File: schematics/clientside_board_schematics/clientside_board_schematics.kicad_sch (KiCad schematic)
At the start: 21 parts, among them J1 Comm Status LED, J2 12V Power Input, J3 UART Connector, J4 12V Output, J5 5V Output, J6 Potentiometer Connector, J7 Fire Button Connector, J8 Keylock Switch Connector, J9 LCD Connector, T1 VXO7805-1000

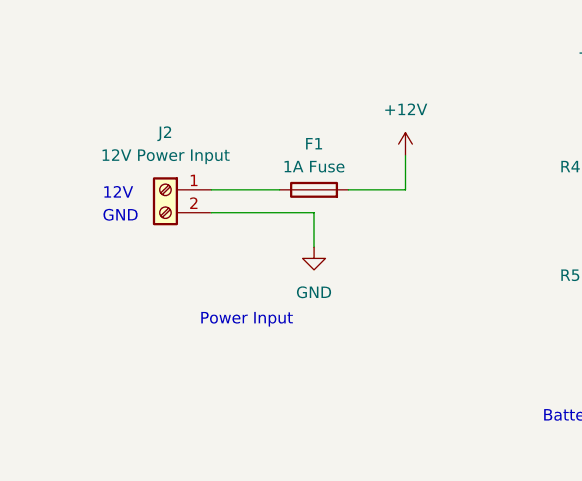
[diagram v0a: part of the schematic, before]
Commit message: Add clientside board routing
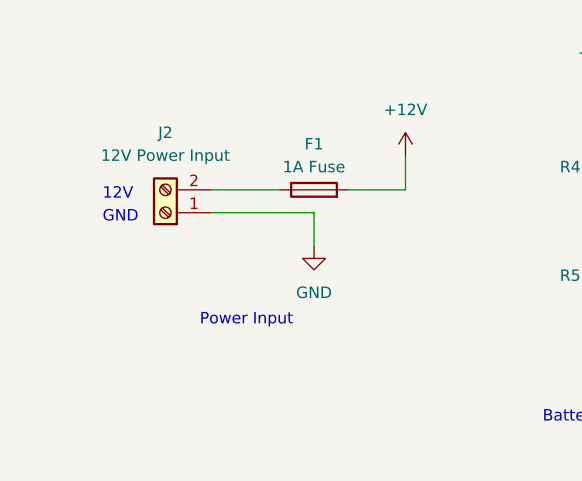
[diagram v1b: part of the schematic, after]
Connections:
- net GND: now also J2.1 (Pin_1); no longer J2.2 (Pin_2)
- net at F1.1: now also J2.2 (Pin_2); no longer J2.1 (Pin_1)
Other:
- moved on the sheet: J2
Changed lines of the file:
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@@
+    (stroke (width 0) (type default))
+  )
+  (wire (pts (xy 50.8 130.81) (xy 53.34 130.81))
+    (stroke (width 0) (type default))
+  )
+  (wire (pts (xy 86.36 44.45) (xy 86.36 45.72))
+    (stroke (width 0) (type default))
+  )
+  (wire (pts (xy 158.75 35.56) (xy 168.91 35.56))
+    (stroke (width 0) (type default))
+  )
+  (wire (pts (xy 139.7 166.37) (xy 139.7 168.91))
+    (stroke (width 0) (type default))
+  )
+  (wire (pts (xy 160.02 91.44) (xy 175.26 91.44))
+    (stroke (width 0) (type default))
+  )
+  (wire (pts (xy 234.95 97.79) (xy 237.49 97.79))
+    (stroke (width 0) (type default))
+  )
+  (wire (pts (xy 233.68 115.57) (xy 237.49 115.57))
+    (stroke (width 0) (type default))
+  )
+  (wire (pts (xy 233.68 110.49) (xy 237.49 110.49))
+    (stroke (width 0) (type default))
+  )
+  (wire (pts (xy 62.23 93.98) (xy 62.23 95.25))
+    (stroke (width 0) (type default))
+  )
+  (wire (pts (xy 113.03 102.87) (xy 113.03 105.41))
+    (stroke (width 0) (type default))
+  )
+  (wire (pts (xy 92.71 116.84) (xy 92.71 123.19))
+    (stroke (width 0) (type default))
+  )
+  (wire (pts (xy 121.92 165.1) (xy 121.92 167.64))
+    (stroke (width 0) (type default))
+  )
+  (wire (pts (xy 123.19 35.56) (xy 133.35 35.56))
+    (stroke (width 0) (type default))
+  )
+  (wire (pts (xy 45.72 91.44) (xy 62.23 91.44))
+    (stroke (width 0) (type default))
+  )
+  (wire (pts (xy 133.35 33.02) (xy 133.35 35.56))
+    (stroke (width 0) (type default))
+  )
+  (wire (pts (xy 234.95 125.73) (xy 234.95 123.19))
+    (stroke (width 0) (type default))
+  )
+  (wire (pts (xy 92.71 96.52) (xy 92.71 105.41))
+    (stroke (width 0) (type default))
+  )
+  (wire (pts (xy 36.83 120.65) (xy 41.91 120.65))
+    (stroke (width 0) (type default))
+  )
+  (wire (pts (xy 214.63 34.29) (xy 229.87 34.29))
+    (stroke (width 0) (type default))
+  )
+  (wire (pts (xy 133.35 38.1) (xy 133.35 41.91))
+    (stroke (width 0) (type default))
+  )
+  (wire (pts (xy 50.8 114.3) (xy 53.34 114.3))
+    (stroke (width 0) (type default))
+  )
+  (wire (pts (xy 50.8 123.19) (xy 53.34 123.19))
+    (stroke (width 0) (type default))
+  )
+  (wire (pts (xy 175.26 86.36) (xy 175.26 83.82))
+    (stroke (width 0) (type default))
+  )
+  (wire (pts (xy 234.95 123.19) (xy 237.49 123.19))
+    (stroke (width 0) (type default))
+  )
+  (wire (pts (xy 168.91 30.48) (xy 168.91 35.56))
+    (stroke (width 0) (type default))
+  )
+  (wire (pts (xy 41.91 125.73) (xy 41.91 130.81))
+    (stroke (width 0) (type default))
+  )
+  (wire (pts (xy 229.87 34.29) (xy 229.87 36.83))
+    (stroke (width 0) (type default))
+  )
+  (wire (pts (xy 121.92 96.52) (xy 121.92 105.41))
     (stroke (width 0) (type default))
   )
   (wire (pts (xy 43.18 43.18) (xy 50.8 43.18))
-    (stroke (width 0) (type default))
-  )
-  (wire (pts (xy 50.8 130.81) (xy 53.34 130.81))
-    (stroke (width 0) (type default))
-  )
-  (wire (pts (xy 86.36 44.45) (xy 86.36 45.72))
-    (stroke (width 0) (type default))
-  )
-  (wire (pts (xy 158.75 35.56) (xy 168.91 35.56))
-    (stroke (width 0) (type default))
-  )
-  (wire (pts (xy 139.7 166.37) (xy 139.7 168.91))
-    (stroke (width 0) (type default))
-  )
-  (wire (pts (xy 160.02 91.44) (xy 175.26 91.44))
-    (stroke (width 0) (type default))
-  )
-  (wire (pts (xy 234.95 97.79) (xy 237.49 97.79))
-    (stroke (width 0) (type default))
-  )
-  (wire (pts (xy 233.68 115.57) (xy 237.49 115.57))
-    (stroke (width 0) (type default))
-  )
-  (wire (pts (xy 233.68 110.49) (xy 237.49 110.49))
-    (stroke (width 0) (type default))
-  )
-  (wire (pts (xy 62.23 93.98) (xy 62.23 95.25))
-    (stroke (width 0) (type default))
-  )
-  (wire (pts (xy 113.03 102.87) (xy 113.03 105.41))
-    (stroke (width 0) (type default))
-  )
-  (wire (pts (xy 92.71 116.84) (xy 92.71 123.19))
-    (stroke (width 0) (type default))
-  )
-  (wire (pts (xy 121.92 165.1) (xy 121.92 167.64))
-    (stroke (width 0) (type default))
-  )
-  (wire (pts (xy 123.19 35.56) (xy 133.35 35.56))
-    (stroke (width 0) (type default))
-  )
-  (wire (pts (xy 45.72 91.44) (xy 62.23 91.44))
-    (stroke (width 0) (type default))
-  )
-  (wire (pts (xy 133.35 33.02) (xy 133.35 35.56))
-    (stroke (width 0) (type default))
-  )
-  (wire (pts (xy 234.95 125.73) (xy 234.95 123.19))
-    (stroke (width 0) (type default))
-  )
-  (wire (pts (xy 92.71 96.52) (xy 92.71 105.41))
-    (stroke (width 0) (type default))
-  )
-  (wire (pts (xy 36.83 120.65) (xy 41.91 120.65))
-    (stroke (width 0) (type default))
-  )
-  (wire (pts (xy 214.63 34.29) (xy 229.87 34.29))
-    (stroke (width 0) (type default))
-  )
-  (wire (pts (xy 133.35 38.1) (xy 133.35 41.91))
-    (stroke (width 0) (type default))
-  )
-  (wire (pts (xy 50.8 114.3) (xy 53.34 114.3))
-    (stroke (width 0) (type default))
-  )
-  (wire (pts (xy 50.8 123.19) (xy 53.34 123.19))
-    (stroke (width 0) (type default))
-  )
-  (wire (pts (xy 175.26 86.36) (xy 175.26 83.82))
-    (stroke (width 0) (type default))
-  )
-  (wire (pts (xy 234.95 123.19) (xy 237.49 123.19))
-    (stroke (width 0) (type default))
-  )
-  (wire (pts (xy 168.91 30.48) (xy 168.91 35.56))
-    (stroke (width 0) (type default))
-  )
-  (wire (pts (xy 41.91 125.73) (xy 41.91 130.81))
-    (stroke (width 0) (type default))
-  )
-  (wire (pts (xy 229.87 34.29) (xy 229.87 36.83))
-    (stroke (width 0) (type default))
-  )
-  (wire (pts (xy 121.92 96.52) (xy 121.92 105.41))
     (stroke (width 0) (type default))
   )
@@
     )
   )
-  (symbol (lib_id "Connector:Screw_Terminal_01x02") (at 38.1 43.18 0) (mirror y) (unit 1)
-    (in_bom yes) (on_board yes) (dnp no) (fields_autoplaced)
+  (symbol (lib_id "Connector:Screw_Terminal_01x02") (at 38.1 45.72 180) (unit 1)
+    (in_bom yes) (on_board yes) (dnp no)
     (property "Reference" "J2" (at 38.1 36.83 0)
       (effects (font (size 1.27 1.27)))
@@
       (effects (font (size 1.27 1.27)))
     )
-    (property "Footprint" "TerminalBlock_Phoenix:TerminalBlock_Phoenix_MKDS-1,5-2-5.08_1x02_P5.08mm_Horizontal" (at 38.1 43.18 0)
-      (effects (font (size 1.27 1.27)) hide)
-    )
-    (property "Datasheet" "~" (at 38.1 43.18 0)
-      (effects (font (size 1.27 1.27)) hide)
-    )
+    (property "Footprint" "TerminalBlock_Phoenix:TerminalBlock_Phoenix_MKDS-1,5-2-5.08_1x02_P5.08mm_Horizontal" (at 38.1 45.72 0)
+      (effects (font (size 1.27 1.27)) hide)
+    )
+    (property "Datasheet" "~" (at 38.1 45.72 0)
+      (effects (font (size 1.27 1.27)) hide)
+    )

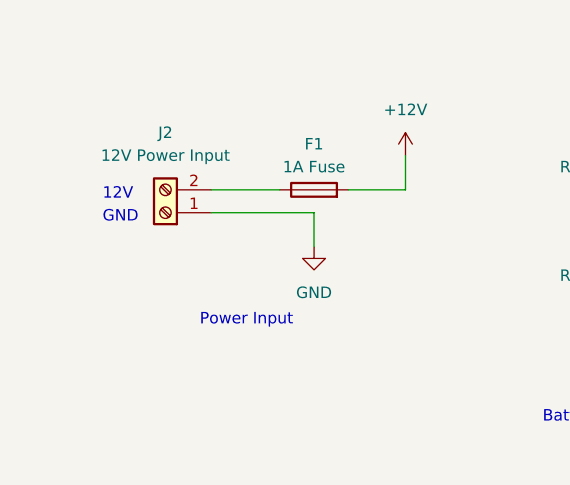
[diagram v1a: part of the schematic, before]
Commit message: Add name to client-side board silkscreen
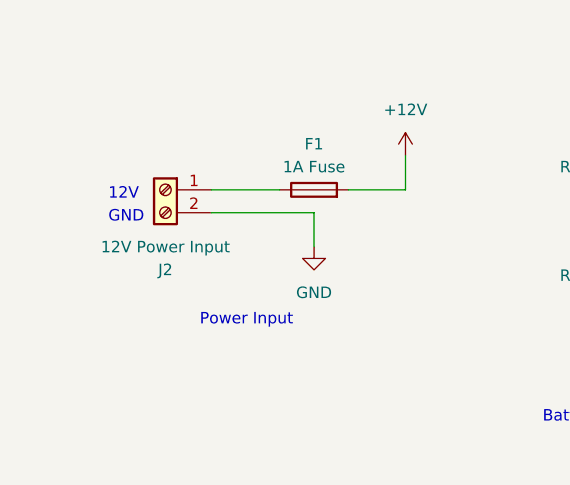
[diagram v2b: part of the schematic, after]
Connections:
- net GND: now also J2.2 (Pin_2); no longer J2.1 (Pin_1)
- net at F1.1: now also J2.1 (Pin_1); no longer J2.2 (Pin_2)
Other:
- moved on the sheet: J2
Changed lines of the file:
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@@
+    (stroke (width 0) (type default))
+  )
+  (wire (pts (xy 43.18 43.18) (xy 50.8 43.18))
     (stroke (width 0) (type default))
   )
@@
     (stroke (width 0) (type default))
   )
+  (wire (pts (xy 43.18 45.72) (xy 54.61 45.72))
+    (stroke (width 0) (type default))
+  )
   (wire (pts (xy 41.91 125.73) (xy 41.91 130.81))
     (stroke (width 0) (type default))
@@
     (stroke (width 0) (type default))
   )
-  (wire (pts (xy 43.18 43.18) (xy 50.8 43.18))
-    (stroke (width 0) (type default))
-  )
   (wire (pts (xy 160.02 86.36) (xy 175.26 86.36))
     (stroke (width 0) (type default))
@@
     (stroke (width 0) (type default))
   )
-  (wire (pts (xy 43.18 45.72) (xy 54.61 45.72))
-    (stroke (width 0) (type default))
-  )
   (wire (pts (xy 210.82 87.63) (xy 237.49 87.63))
     (stroke (width 0) (type default))
@@
     (effects (font (size 1.27 1.27)) (justify left bottom))
   )
-  (text "GND" (at 31.115 46.99 0)
-    (effects (font (size 1.27 1.27)) (justify left bottom))
-  )
-  (text "12V" (at 31.115 44.45 0)
+  (text "GND" (at 31.75 46.99 0)
+    (effects (font (size 1.27 1.27)) (justify left bottom))
+  )
+  (text "12V" (at 31.75 44.45 0)
     (effects (font (size 1.27 1.27)) (justify left bottom))
   )
@@
     )
   )
-  (symbol (lib_id "Connector:Screw_Terminal_01x02") (at 38.1 45.72 180) (unit 1)
+  (symbol (lib_id "Connector:Screw_Terminal_01x02") (at 38.1 43.18 0) (mirror y) (unit 1)
     (in_bom yes) (on_board yes) (dnp no)
-    (property "Reference" "J2" (at 38.1 36.83 0)
-      (effects (font (size 1.27 1.27)))
-    )
-    (property "Value" "12V Power Input" (at 38.1 39.37 0)
-      (effects (font (size 1.27 1.27)))
-    )
-    (property "Footprint" "TerminalBlock_Phoenix:TerminalBlock_Phoenix_MKDS-1,5-2-5.08_1x02_P5.08mm_Horizontal" (at 38.1 45.72 0)
-      (effects (font (size 1.27 1.27)) hide)
-    )
-    (property "Datasheet" "~" (at 38.1 45.72 0)
-      (effects (font (size 1.27 1.27)) hide)
-    )
+    (property "Reference" "J2" (at 38.1 52.07 0)
+      (effects (font (size 1.27 1.27)))
+    )
+    (property "Value" "12V Power Input" (at 38.1 49.53 0)
+      (effects (font (size 1.27 1.27)))
+    )
+    (property "Footprint" "TerminalBlock_Phoenix:TerminalBlock_Phoenix_MKDS-1,5-2-5.08_1x02_P5.08mm_Horizontal" (at 38.1 43.18 0)
+      (effects (font (size 1.27 1.27)) hide)
+    )
+    (property "Datasheet" "~" (at 38.1 43.18 0)
+      (effects (font (size 1.27 1.27)) hide)
+    )
